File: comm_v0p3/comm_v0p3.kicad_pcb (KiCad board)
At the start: 2 copper layers, 40 x 40 mm, 14 parts, among them IC5 ATMEGA328-A, M1 CONN_1, M2 CONN_1, P1 CONN15, P2 CONN15, P4 CONN_2X2, P5 CONN_2X2, P6 CONN_2X2, P7 CONN_2X2, P8 CONN_2, X5 CER_RESO

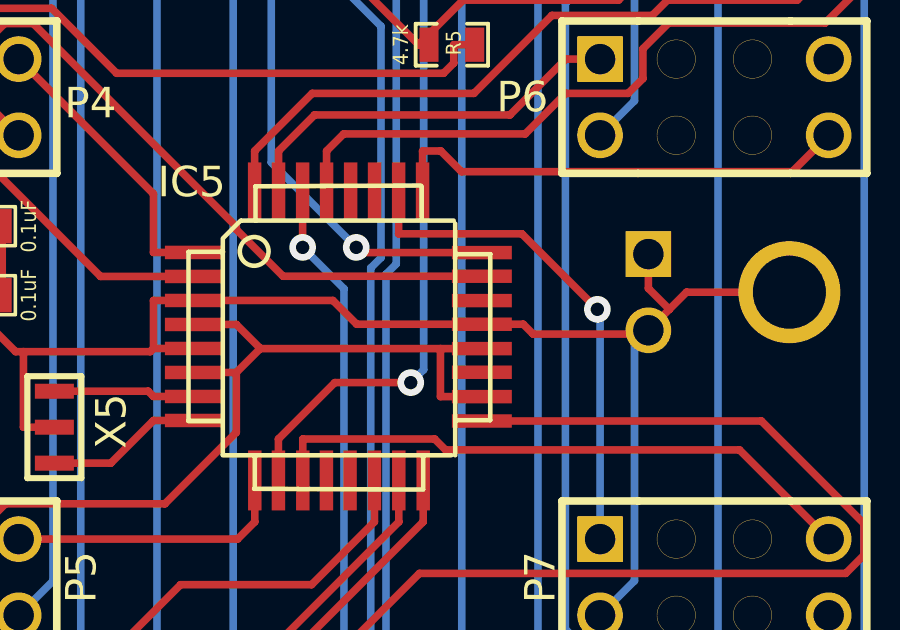
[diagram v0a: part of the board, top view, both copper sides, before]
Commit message: convert comm_v0p3 to KiCad7
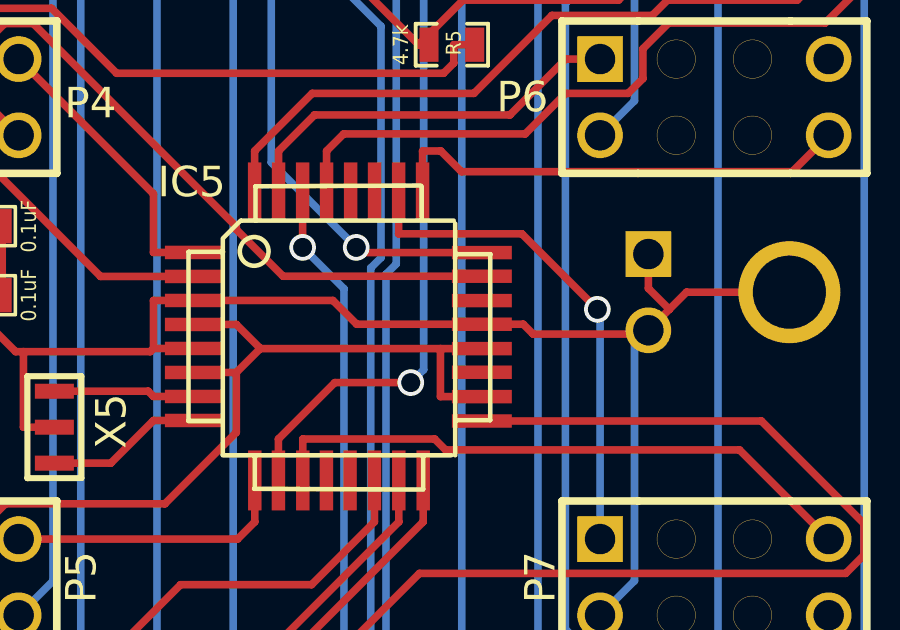
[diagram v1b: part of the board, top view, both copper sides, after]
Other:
- net class Default removed
